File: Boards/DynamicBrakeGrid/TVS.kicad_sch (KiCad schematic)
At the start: 16 parts

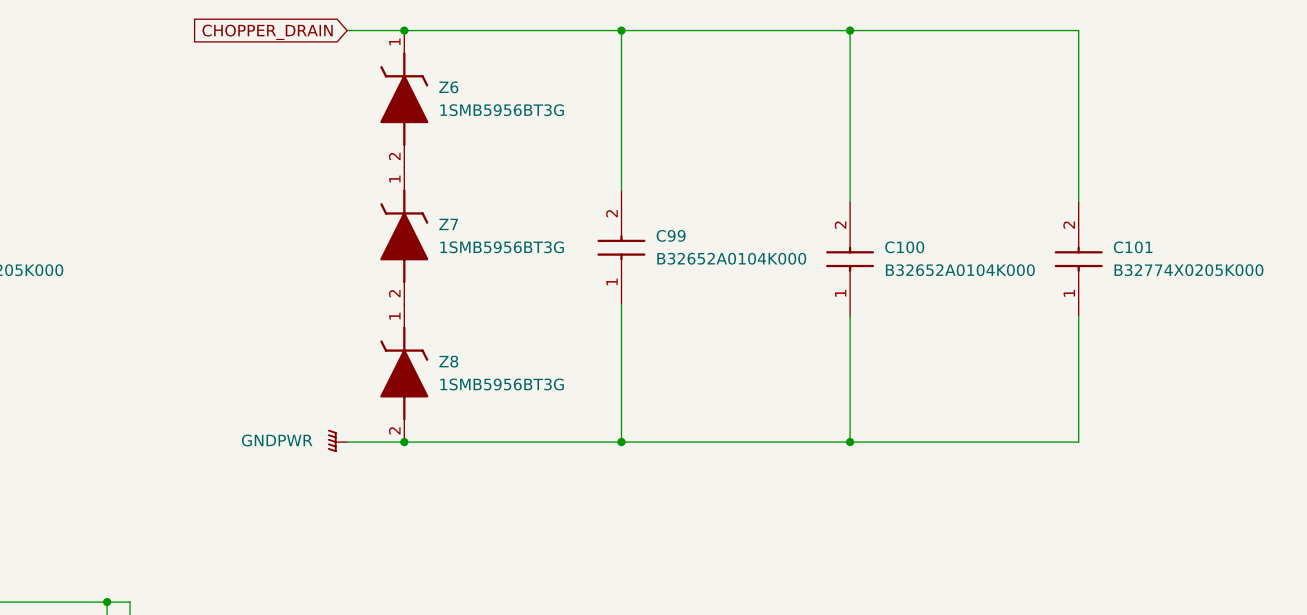
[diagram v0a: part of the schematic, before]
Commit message: Update Dynamic Brake Board
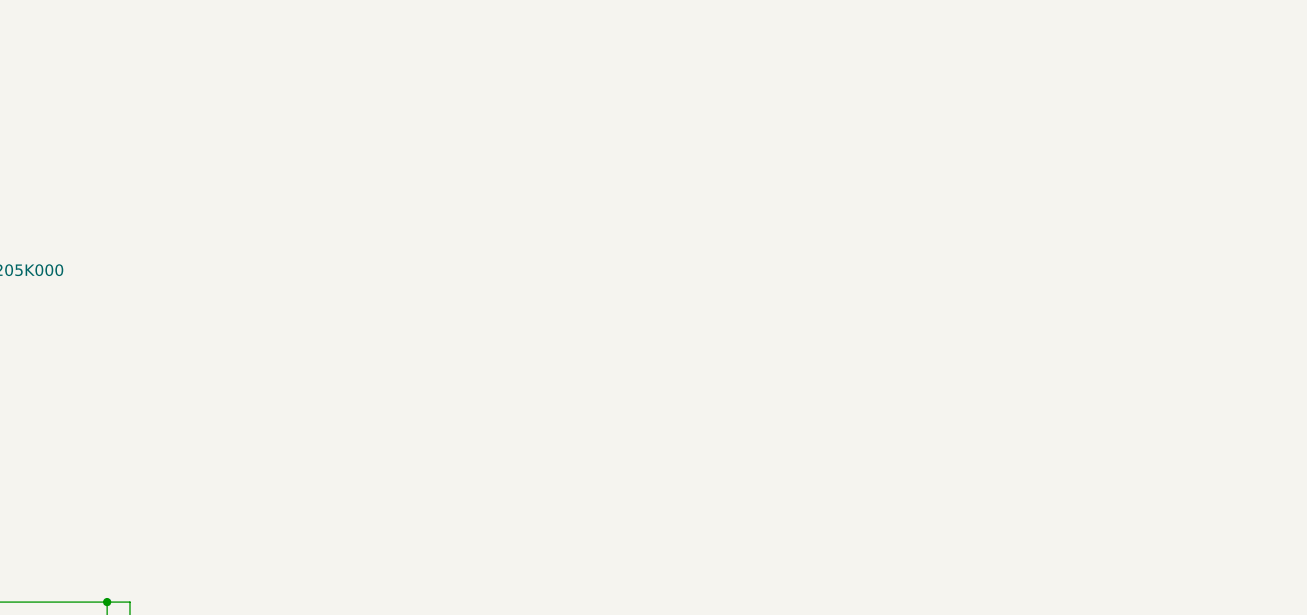
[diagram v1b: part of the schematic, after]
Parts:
- removed C100, C99: B32652A0104K000, InverterCom:B32652__18_x_9_, symbol InverterCom:B32652A0104K000
- removed C101: B32774X0205K000, InverterCom:B32774X__31.5_x_12.5_, symbol InverterCom:B32774X0205K000
- removed Z6, Z7, Z8: 1SMB5956BT3G, InverterCom:DIOM5436X247N, symbol InverterCom:1SMB5956BT3G
